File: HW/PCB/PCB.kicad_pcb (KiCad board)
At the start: 2 copper layers, 74 x 44 mm, 48 parts, among them J1 USB4105-GF-A, J2 DC_Jack, J4 Micro_SD_Card_Det_Hirose_DM3AT, Q1 2PC4081R, Q2 2PC4081R, SW1 ssss213202, SW2 SKRPACE010, SW3 SKRPACE010, U1 SCD40-D-R2, U2 FT231XS, U3 LT1963ES8-3.3, U4 ESP32-S3-WROOM-1, U5 BME280, U6 AQM0802A-RN-GBW, Y1 FC-135

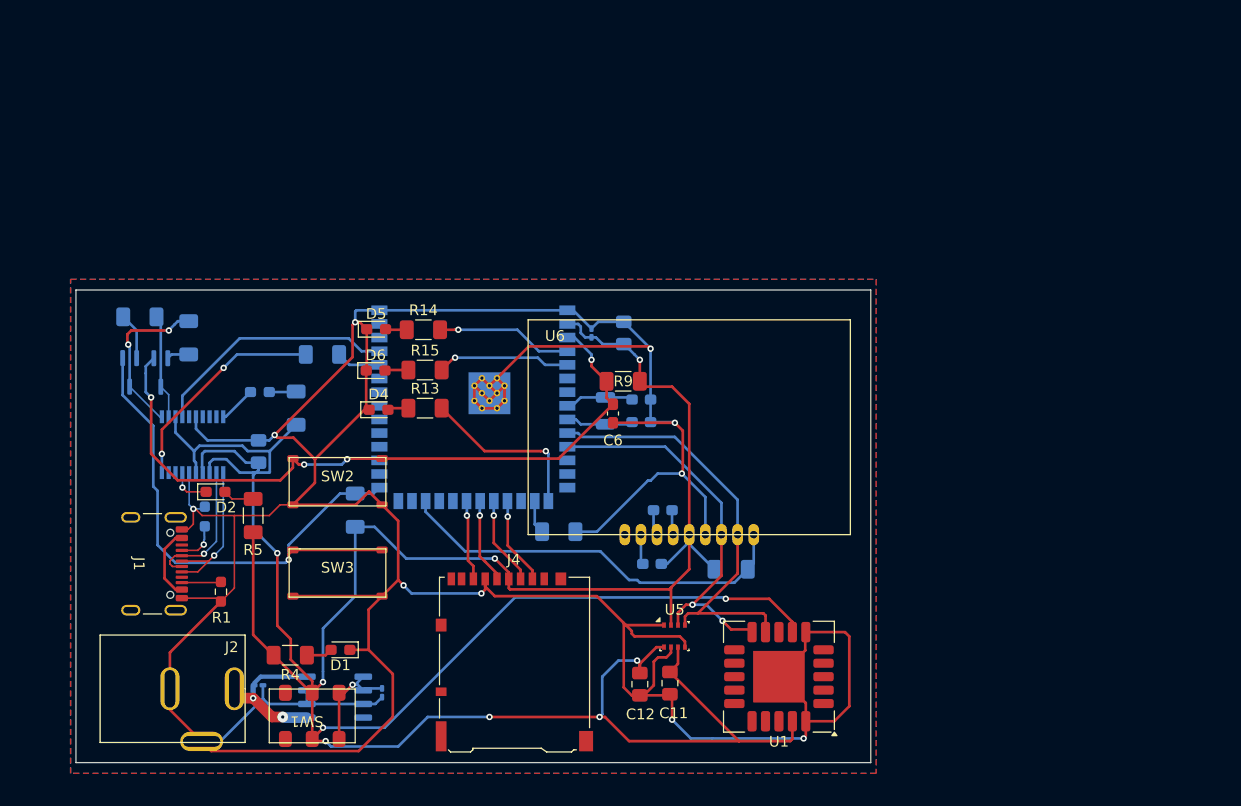
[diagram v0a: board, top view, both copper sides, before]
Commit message: modify PCB layout
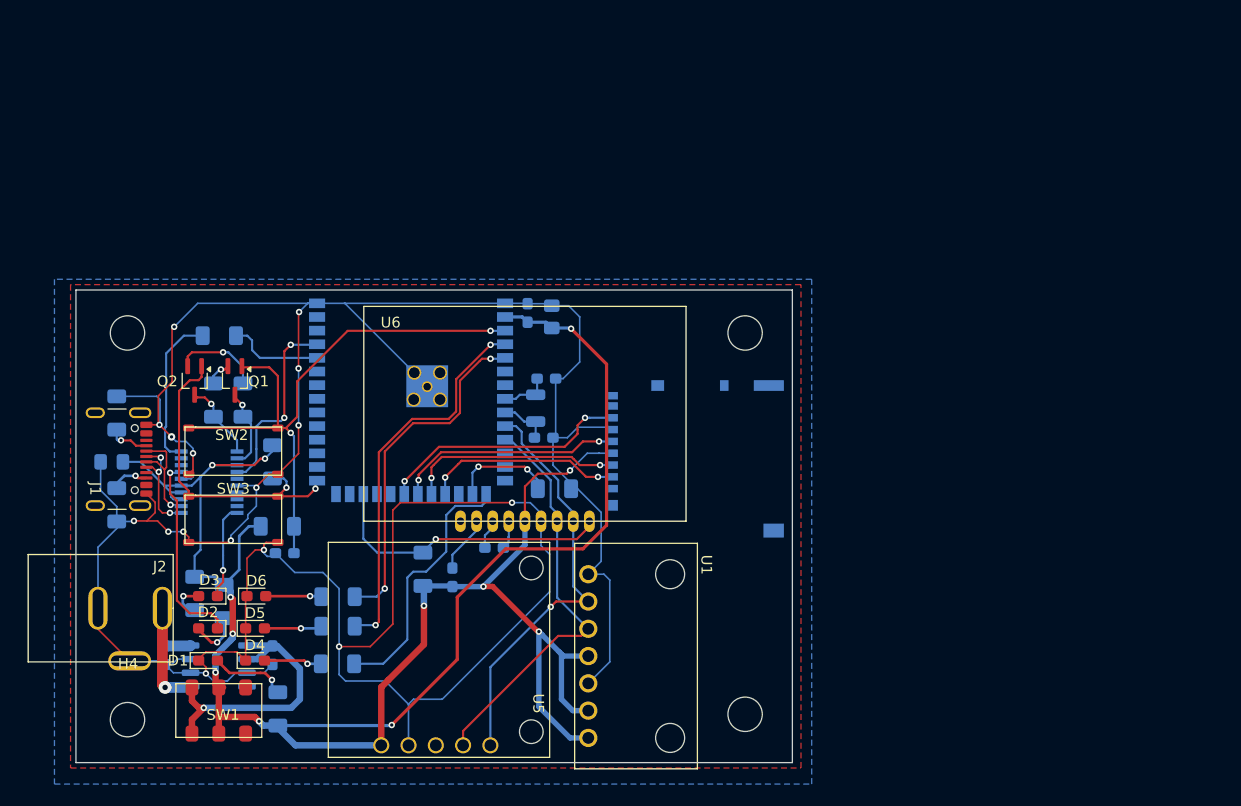
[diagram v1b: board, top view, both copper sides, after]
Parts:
- removed C11, C12: 0.1uF, Capacitor_SMD:C_0805_2012Metric_Pad1.18x1.45mm_HandSolder
- added H1: M3_MountHoll, MountingHole:MountingHole_3.2mm_M3, F.Cu at (93.3, 74.0)
- added H2: M3_MountHoll, MountingHole:MountingHole_3.2mm_M3, F.Cu at (150.8, 74.0)
- added H3: M3_MountHoll, MountingHole:MountingHole_3.2mm_M3, F.Cu at (150.8, 109.5)
- added H4: M3_MountHoll, MountingHole:MountingHole_3.2mm_M3, F.Cu at (93.3, 110.0)
- C1, C2, C5: footprint Capacitor_SMD:C_0201_0603Metric_Pad0.64x0.40mm_HandSolder -> Capacitor_SMD:C_0603_1608Metric_Pad1.08x0.95mm_HandSolder
- C6, J4, R13, R14, R15, R4, R5, R9: moved to B.Cu
- D3, Q1, Q2: moved to F.Cu
- R1: footprint Resistor_SMD:R_0603_1608Metric_Pad0.98x0.95mm_HandSolder -> Resistor_SMD:R_1206_3216Metric_Pad1.30x1.75mm_HandSolder; moved to B.Cu
- R2: footprint Resistor_SMD:R_0603_1608Metric_Pad0.98x0.95mm_HandSolder -> Resistor_SMD:R_1206_3216Metric_Pad1.30x1.75mm_HandSolder
- U1: value SCD40-D-R2 -> ~; footprint Sensor:Sensirion_SCD4x-1EP_10.1x10.1mm_P1.25mm_EP4.8x4.8mm -> mylib:BME280_SwitchScience
- U4: footprint RF_Module:ESP32-S3-WROOM-1 -> mylib:ESP32-S3-WROOM-1
- U5: value BME280 -> SCD40; footprint Package_LGA:Bosch_LGA-8_2.5x2.5mm_P0.65mm_ClockwisePinNumbering -> mylib:SCD40_Conta
- moved R9 34.9 mm to (107.2, 92.0), turned to 180 degrees
- moved C6 33.2 mm to (107.9, 94.5), turned to 180 degrees
- moved D5 30.0 mm to (105.2, 101.5)
- moved R14 28.7 mm to (112.9, 101.3)
- moved R12 28.7 mm to (120.8, 96.0), turned to -90 degrees
- moved D4 26.0 mm to (105.2, 104.5)
- moved J4 25.3 mm to (146.1, 85.7), turned to -90 degrees
- moved R13 25.2 mm to (112.8, 104.8)
- moved U5 24.4 mm to (122.0, 112.4), turned to -90 degrees
- moved D6 23.8 mm to (105.3, 98.5)
- moved R15 22.6 mm to (112.9, 98.5)
- moved R6 19.7 mm to (99.5, 98.2), turned to 90 degrees
- moved D3 19.6 mm to (100.8, 98.5), turned to 180 degrees
- moved C9 18.6 mm to (123.5, 96.8), turned to 90 degrees
- moved U1 17.9 mm to (136.2, 104.1), turned to -90 degrees
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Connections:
- J1 pad A4: VBUS -> unconnected-(J1-VBUS-PadA4)_2
- J1 pad A9: VBUS -> unconnected-(J1-VBUS-PadA4)
- J1 pad B4: VBUS -> unconnected-(J1-VBUS-PadA4)_1
- J1 pad B9: VBUS -> unconnected-(J1-VBUS-PadA4)_3
- U1 pad 1: (no net) -> GND
- U1 pad 2: (no net) -> ESP32_IO17_SCL
- U1 pad 3: (no net) -> ESP32_IO18_SDA
- U1 pad 4: (no net) -> +3V3
- U1 pad 5: (no net) -> GND
- U1 pad 6: GND -> +3V3
- U5 pad 1: GND -> ESP32_IO17_SCL
- U5 pad 2: +3V3 -> ESP32_IO18_SDA
- U5 pad 3: ESP32_IO18_SDA -> unconnected-(U5-IO4-Pad3)
- U5 pad 4: ESP32_IO17_SCL -> GND
- U5 pad 5: GND -> +3V3
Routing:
- net +3V3: track 300.2 -> 217.2 mm, vias 10 -> 12
- net GND: track 372.9 -> 309.0 mm, vias 10 -> 16
- net ESP32_IO0: track 53.2 -> 29.9 mm, vias 1 -> 2
- net ESP32_IO4: track 12.7 -> 35.9 mm, vias 1 -> 2
- net ESP32_IO5: track 12.5 -> 32.4 mm, vias 1 -> 2
- net SW_1: track 10.2 -> 26.3 mm
- net ESP32_IO13_SPI_MISO: track 7.51 -> 23.4 mm, vias 1 -> 2
- net CBUS1: track 3.77 -> 18.5 mm
- net ESP32_IO12_SPI_SCK: track 7.93 -> 21.1 mm, vias 1 -> 2
- net ESP32_IO11_SPI_MOSI: track 8.29 -> 20.0 mm, vias 1 -> 2
- net ESP32_IO47: track 37.7 -> 27.3 mm, vias 0 -> 1
- net ESP32_IO10_SPI_CS: track 8.21 -> 18.3 mm, vias 1 -> 2
- net ESP32_EN: track 65.7 -> 55.7 mm, vias 4 -> 2
- net ESP32_IO3: track 16.1 -> 24.6 mm, vias 1 -> 0
- net DTR: track 15.5 -> 7.33 mm, vias 2 -> 1
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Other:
- board size 74 x 44 mm -> 66.7 x 44 mm

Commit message: add PMIC
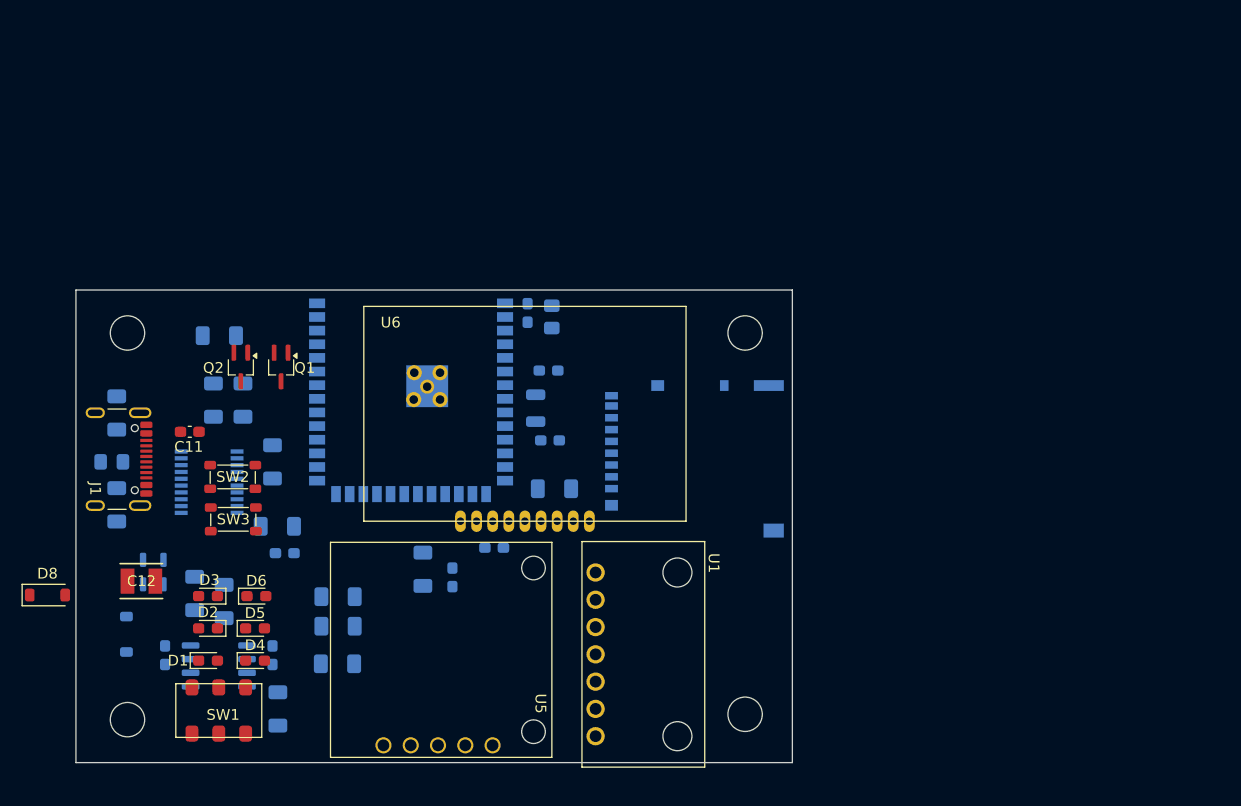
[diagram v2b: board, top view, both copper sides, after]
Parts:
- removed J2: DC_Jack, mylib:MJ-179PH
- added C11: 0.01uF, Capacitor_SMD:C_0603_1608Metric_Pad1.08x0.95mm_HandSolder, F.Cu at (99.1, 83.2)
- added C12: 22uF, TAJ_SMD:TAJB_AVX, F.Cu at (94.6, 97.1)
- added D7: RB161MM-20, Diode_SMD:D_SOD-123, B.Cu at (93.2, 102.0)
- added D8: RB161MM-20, Diode_SMD:D_SOD-123, F.Cu at (85.8, 98.4)
- added U7: TPS2065DDBVR, Package_TO_SOT_SMD:SOT-23-5, B.Cu at (95.7, 96.3)
- U1: value ~ -> BME280
- moved Q1 4.48 mm to (107.6, 77.2)
- moved Q2 4.48 mm to (103.8, 77.2)
- moved SW2 2.40 mm to (103.1, 87.4)
- moved C7 0.78 mm to (132.5, 77.5)
- moved U1 0.70 mm to (136.9, 103.9)
- moved C8 0.64 mm to (132.6, 84.0)
- moved U5 0.20 mm to (122.2, 112.4)
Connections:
- C1 pad 1: VDD -> SW_1
- C2 pad 1: SW_1 -> VDD
- C4 pad 1: +3V3 -> GND
- C4 pad 2: GND -> +3V3
- C5 pad 1: +3V3 -> GND
- C5 pad 2: GND -> +3V3
- J1 pad A4: unconnected-(J1-VBUS-PadA4)_2 -> VBUS
- J1 pad A9: unconnected-(J1-VBUS-PadA4) -> VBUS
- J1 pad B4: unconnected-(J1-VBUS-PadA4)_1 -> VBUS
- J1 pad B9: unconnected-(J1-VBUS-PadA4)_3 -> VBUS
- U3 pad 5: VDD -> VDDA
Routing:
- net GND: track 309.0 -> 0.00 mm, vias 16 -> 0
- net +3V3: track 217.2 -> 0.00 mm, vias 12 -> 0
- net ESP32_EN: track 55.7 -> 0.00 mm, vias 2 -> 0
- net ESP32_IO17_SCL: track 39.1 -> 0.00 mm, vias 1 -> 0
- net ESP32_IO18_SDA: track 38.0 -> 0.00 mm
- net ESP32_IO4: track 35.9 -> 0.00 mm, vias 2 -> 0
- net ESP32_IO5: track 32.4 -> 0.00 mm, vias 2 -> 0
- net ESP32_IO0: track 29.9 -> 0.00 mm, vias 2 -> 0
- net ESP32_IO47: track 27.3 -> 0.00 mm, vias 1 -> 0
- net SW_1: track 26.3 -> 0.00 mm, vias 1 -> 0
- net ESP32_IO3: track 24.6 -> 0.00 mm
- net ESP32_IO13_SPI_MISO: track 23.4 -> 0.00 mm, vias 2 -> 0
- net ESP32_IO12_SPI_SCK: track 21.1 -> 0.00 mm, vias 2 -> 0
- net ESP32_IO11_SPI_MOSI: track 20.0 -> 0.00 mm, vias 2 -> 0
- net CBUS1: track 18.5 -> 0.00 mm, vias 1 -> 0
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- removed copper zone on B.Cu, net GND
- removed copper zone on F.Cu, net GND

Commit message: modify PCB design pattern
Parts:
- C11, C12, D8: moved to B.Cu
- moved C11 11.6 mm to (96.7, 94.5), turned to -90 degrees
- moved C3 11.4 mm to (99.8, 94.2), turned to 0 degrees
- moved D7 10.6 mm to (100.5, 109.8), turned to 0 degrees
- moved C2 9.80 mm to (97.0, 103.8)
- moved C1 9.80 mm to (106.6, 104.1)
- moved D8 9.15 mm to (95.0, 98.2), turned to 180 degrees
- moved C12 4.63 mm to (93.5, 101.6), turned to 180 degrees
- moved SW1 3.11 mm to (102.4, 109.5)
- moved U7 2.78 mm to (93.4, 94.8), turned to 0 degrees
- moved C7 1.61 mm to (133.3, 78.9), turned to 90 degrees
- moved C8 1.12 mm to (133.3, 83.1), turned to -90 degrees
- turned C4 to -90 degrees
- turned C5 to -90 degrees
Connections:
- U3 pad 5: VDDA -> VDD
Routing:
- net GND: track 0.00 -> 261.3 mm, vias 0 -> 13
- net +3V3: track 0.00 -> 181.7 mm, vias 0 -> 10
- net ESP32_EN: track 0.00 -> 49.8 mm, vias 0 -> 2
- net ESP32_IO4: track 0.00 -> 42.6 mm, vias 0 -> 2
- net ESP32_IO17_SCL: track 0.00 -> 39.2 mm
- net ESP32_IO18_SDA: track 0.00 -> 39.0 mm
- net ESP32_IO5: track 0.00 -> 38.7 mm, vias 0 -> 2
- net SW_1: track 0.00 -> 28.1 mm, vias 0 -> 2
- net ESP32_IO47: track 0.00 -> 27.3 mm, vias 0 -> 1
- net ESP32_IO0: track 0.00 -> 26.3 mm, vias 0 -> 4
- net ESP32_IO3: track 0.00 -> 25.3 mm, vias 0 -> 2
- net ESP32_IO13_SPI_MISO: track 0.00 -> 24.9 mm, vias 0 -> 2
- net ESP32_IO11_SPI_MOSI: track 0.00 -> 24.5 mm, vias 0 -> 2
- net ESP32_IO12_SPI_SCK: track 0.00 -> 24.5 mm, vias 0 -> 2
- net VBUS: track 0.00 -> 23.4 mm, vias 0 -> 2
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
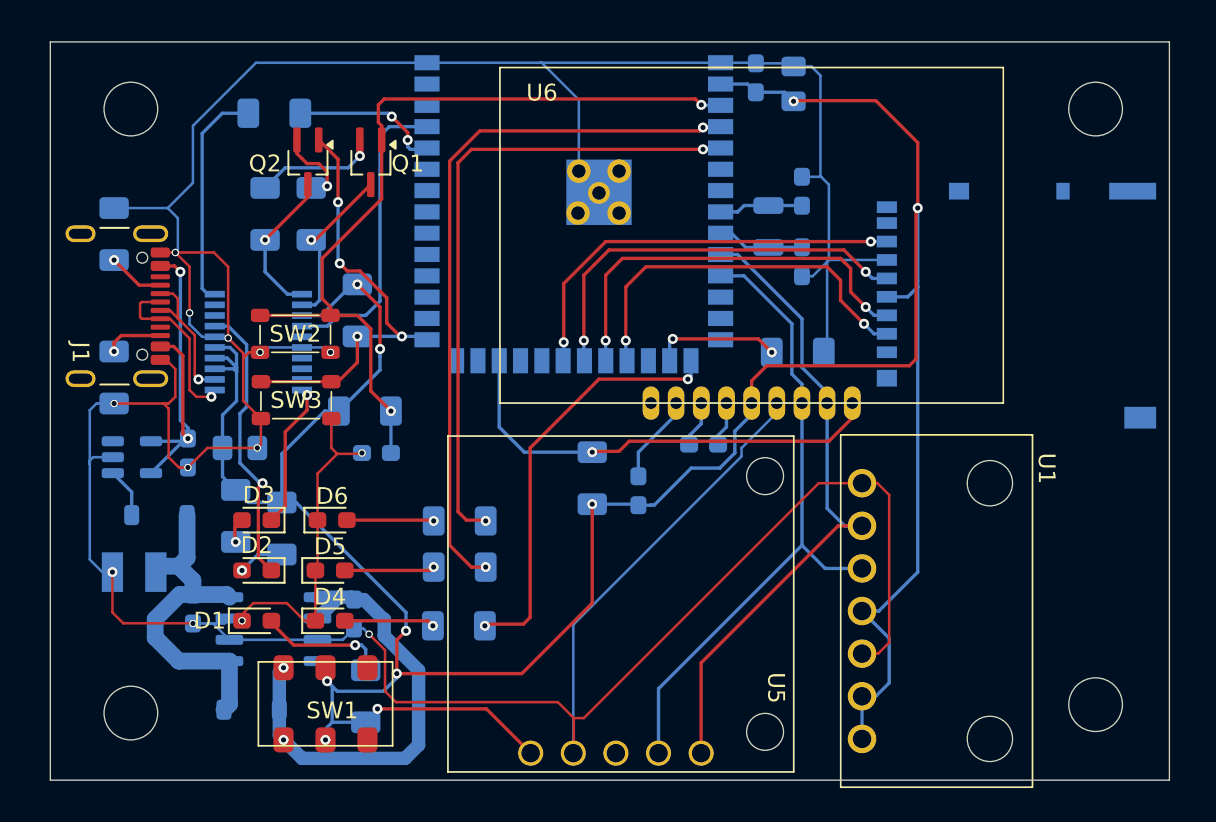
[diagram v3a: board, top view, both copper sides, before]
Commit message: modify PCB layout
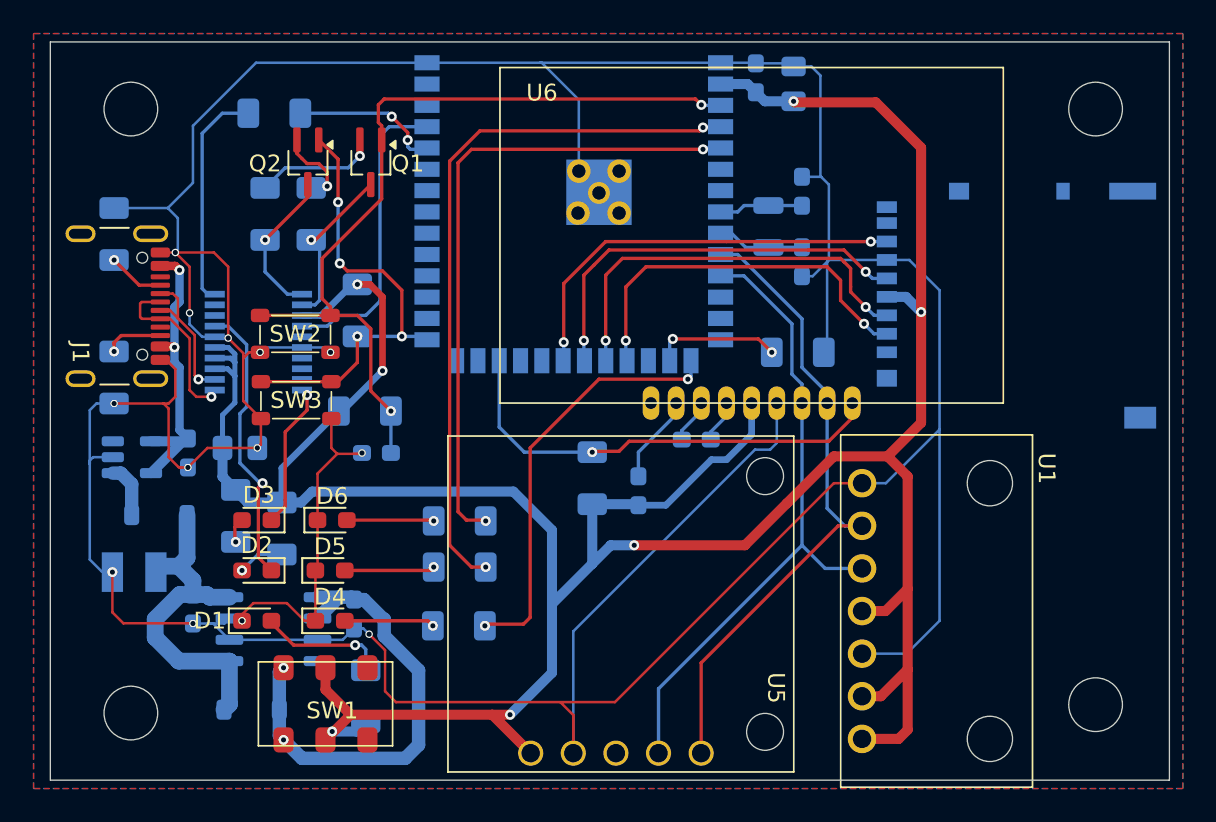
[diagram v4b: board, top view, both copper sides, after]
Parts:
- moved C10 0.53 mm to (127.0, 93.7)
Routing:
- net GND: track 261.3 -> 284.7 mm
- net +3V3: track 181.7 -> 189.8 mm, vias 10 -> 7
- net VBUS: track 23.4 -> 18.2 mm
- net ESP32_IO0: track 26.3 -> 27.0 mm
- added copper zone on B.Cu, net GND
- added copper zone on F.Cu, net GND
